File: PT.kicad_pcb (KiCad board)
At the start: 4 copper layers, 67 x 68 mm, 111 parts, among them J1 Conn_02x05_Odd_Even, J10 Conn_02x01, J11 Screw_Terminal_01x02, J2 USB_C_Receptacle_USB2.0_16P, J3 Conn_02x01, J4 Conn_02x01, J5 Screw_Terminal_01x05, J6 RJ45_Hanrun_HR911105A_Horizon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, J7 Conn_02x01, J8 Conn_02x01, J9 Conn_02x01, SW1 SKRPANE010, U1 USBLC6-2SC6, U2 STM32H563RIVx, U3 AP2112K-3.3, U4 TJA1042T-3, U5 LAN8742A, U6 ADS131A04, Y1 25 MHz, Y2 25 MHz, Y3 16.384 MHz

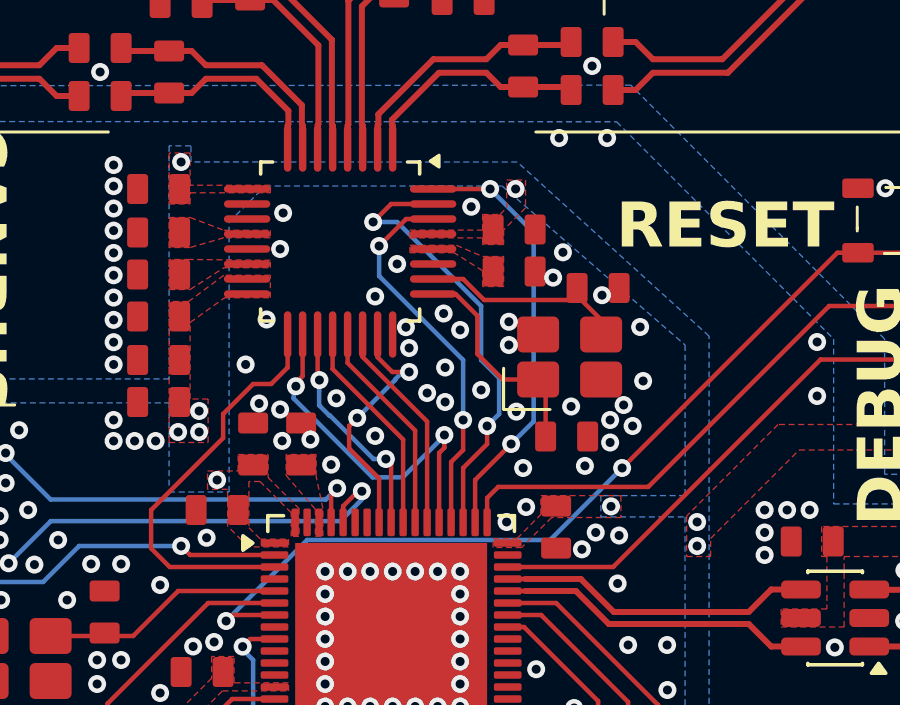
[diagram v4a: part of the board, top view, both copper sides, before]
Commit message: Use static configurations for ADC instead of using MCU for pullups/downs
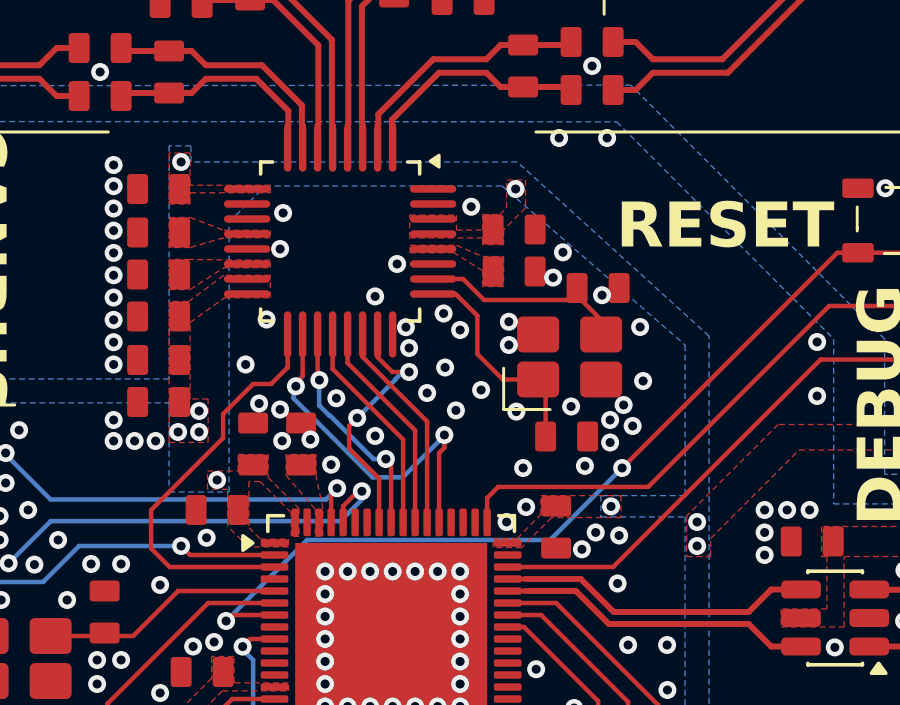
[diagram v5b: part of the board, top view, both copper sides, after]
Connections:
- net ETH_CRS_DV renamed /Connectivity/ETH_CRS_DV
- net ETH_MDC renamed /Connectivity/ETH_MDC
- net ETH_MDIO renamed /Connectivity/ETH_MDIO
- net ETH_REF_CLK renamed /Connectivity/ETH_REF_CLK
- net ETH_RXD0 renamed /Connectivity/ETH_RXD0
- net ETH_RXD1 renamed /Connectivity/ETH_RXD1
- net ETH_TXD0 renamed /Connectivity/ETH_TXD0
- net ETH_TXD1 renamed /Connectivity/ETH_TXD1
- net ETH_TX_EN renamed /Connectivity/ETH_TX_EN
- net ETH_~{RST} renamed /Connectivity/ETH_~{RST}
- net FDCAN_RX renamed /Connectivity/FDCAN_RX
- net FDCAN_STDBY renamed /Connectivity/FDCAN_STDBY
- net FDCAN_TX renamed /Connectivity/FDCAN_TX
- net MISO renamed /Analog/MISO
- net MOSI renamed /Analog/MOSI
- net SCLK renamed /Analog/SCLK
- net ~{ADC_RESET} renamed /Analog/~{ADC_RESET}
- net ~{CS} renamed /Analog/~{CS}
- net ~{DONE} renamed /Analog/~{DONE}
- net ~{DRDY} renamed /Analog/~{DRDY}
- U2 pad 53: M2 -> unconnected-(U2-PA15(JTDI)-Pad53)
- U2 pad 54: M1 -> unconnected-(U2-PC10-Pad54)
- U2 pad 55: M0 -> unconnected-(U2-PC11-Pad55)
- U6 pad 30: M0 -> +3.3V
- U6 pad 31: M1 -> GND
- U6 pad 32: M2 -> GND
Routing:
- net M1: track 15.0 -> 0.00 mm, vias 2 -> 0
- net M2: track 14.4 -> 0.00 mm, vias 2 -> 0
- net M0: track 12.7 -> 0.00 mm, vias 2 -> 0

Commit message: holy hell 2 adcs
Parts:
- added C43: 10nF, APRLPrints:C_0603, F.Cu at (106.9, 103.5)
- added C44: 100nF, APRLPrints:C_0603, F.Cu at (111.5, 120.0)
- added C45: 100nF, APRLPrints:C_0603, F.Cu at (113.3, 107.4)
- added C46: 100nF, APRLPrints:C_0603, F.Cu at (116.3, 120.0)
- added C47: 100nF, APRLPrints:C_0603, F.Cu at (117.9, 120.0)
- added C48: 1uF, APRLPrints:C_0603, F.Cu at (119.5, 120.0)
- added C49: 1uF, APRLPrints:C_0603, F.Cu at (113.1, 120.0)
- added C50: 10nF, APRLPrints:C_0603, F.Cu at (106.7, 110.2)
- added C51: 1uF, APRLPrints:C_0603, F.Cu at (114.7, 120.0)
- added C52: 1uF, APRLPrints:C_0603, F.Cu at (114.9, 107.4)
- added C53: 10nF, APRLPrints:C_0603, F.Cu at (106.7, 117.1)
- added C54: 30pF, APRLPrints:C_0603, F.Cu at (117.9, 105.3)
- added C55: 30pF, APRLPrints:C_0603, F.Cu at (120.3, 108.1)
- added C56: 10nF, APRLPrints:C_0603, F.Cu at (106.7, 124.0)
- added F4: 100mA Hold, APRLPrints:Fuse_0805_2012Metric, F.Cu at (120.5, 73.3)
- added F5: 500mA, APRLPrints:Fuse_0805_2012Metric, F.Cu at (170.9, 85.0)
- added J12: Conn_01x04, Connector_PinHeader_2.54mm:PinHeader_1x04_P2.54mm_Vertical, F.Cu at (147.1, 99.1)
- added J13: Conn_02x01, TerminalBlock_Phoenix:TerminalBlock_Phoenix_MPT-0,5-2-2.54_1x02_P2.54mm_Horizontal, F.Cu at (96.8, 102.2)
- added J14: Conn_02x01, TerminalBlock_Phoenix:TerminalBlock_Phoenix_MPT-0,5-2-2.54_1x02_P2.54mm_Horizontal, F.Cu at (96.8, 108.9)
- added J15: Conn_02x01, TerminalBlock_Phoenix:TerminalBlock_Phoenix_MPT-0,5-2-2.54_1x02_P2.54mm_Horizontal, F.Cu at (96.8, 115.8)
- added J16: Conn_02x01, TerminalBlock_Phoenix:TerminalBlock_Phoenix_MPT-0,5-2-2.54_1x02_P2.54mm_Horizontal, F.Cu at (96.8, 122.8)
- added J17: Screw_Terminal_01x02, TerminalBlock_Phoenix:TerminalBlock_Phoenix_MPT-0,5-2-2.54_1x02_P2.54mm_Horizontal, F.Cu at (128.5, 77.4)
- added J18: Conn_01x05, Connector_PinHeader_2.54mm:PinHeader_1x05_P2.54mm_Vertical, F.Cu at (157.4, 103.3)
- added NT5: NetTie_2, NetTie:NetTie-2_SMD_Pad0.5mm, F.Cu at (102.1, 102.1)
- added NT6: NetTie_2, NetTie:NetTie-2_SMD_Pad0.5mm, F.Cu at (102.1, 108.7)
- added NT7: NetTie_2, NetTie:NetTie-2_SMD_Pad0.5mm, F.Cu at (102.1, 115.7)
- added NT8: NetTie_2, NetTie:NetTie-2_SMD_Pad0.5mm, F.Cu at (102.1, 122.5)
- added R32: 100R, APRLPrints:R_0603, F.Cu at (104.7, 104.2)
- added R33: 100R, APRLPrints:R_0805, F.Cu at (102.1, 103.5)
- added R34: 100R, APRLPrints:R_0603, F.Cu at (104.7, 102.7)
- added R35: 100R, APRLPrints:R_0603, F.Cu at (104.5, 111.0)
- added R36: 100R, APRLPrints:R_0805, F.Cu at (102.1, 110.2)
- added R37: 100R, APRLPrints:R_0603, F.Cu at (104.5, 109.4)
- added R38: 100R, APRLPrints:R_0603, F.Cu at (104.5, 117.9)
- added R39: 100R, APRLPrints:R_0805, F.Cu at (102.1, 117.0)
- added R40: 100R, APRLPrints:R_0603, F.Cu at (104.5, 116.3)
- added R41: 100R, APRLPrints:R_0603, F.Cu at (104.5, 124.8)
- added R42: 100R, APRLPrints:R_0805, F.Cu at (102.1, 124.0)
- added R43: 100R, APRLPrints:R_0603, F.Cu at (104.5, 123.2)
- added R44: 10k, APRLPrints:R_0603, F.Cu at (144.5, 98.5)
- added R45: 10k, APRLPrints:R_0603, F.Cu at (142.9, 97.5)
- added U7: ADS131A04, libpt:QFP-32_5x5_Pitch0.5mm, F.Cu at (115.3, 113.7)
- added Y4: 16.384 MHz, APRLPrints:3225-4P-L, F.Cu at (120.5, 105.1)
- F2: value 100mA Hold -> 500mA
- J11: value Screw_Terminal_01x02 -> Conn_02x01
- J3: value Conn_02x01 -> Screw_Terminal_01x02; footprint Connector_PinHeader_2.54mm:PinHeader_2x01_P2.54mm_Vertical -> TerminalBlock_Phoenix:TerminalBlock_Phoenix_MPT-0,5-2-2.54_1x02_P2.54mm_Horizontal
- J5: value Screw_Terminal_01x05 -> Conn_02x01; footprint TerminalBlock_Phoenix:TerminalBlock_Phoenix_MPT-0,5-5-2.54_1x05_P2.54mm_Horizontal -> Connector_PinHeader_2.54mm:PinHeader_2x01_P2.54mm_Vertical
- J6: value RJ45_Hanrun_HR911105A_Horizontal -> Screw_Terminal_01x05; footprint Connector_RJ:RJ45_Hanrun_HR911105A_Horizontal -> TerminalBlock_Phoenix:TerminalBlock_Phoenix_MPT-0,5-5-2.54_1x05_P2.54mm_Horizontal
- J7: value Conn_02x01 -> RJ45_Hanrun_HR911105A_Horizontal; footprint TerminalBlock_Phoenix:TerminalBlock_Phoenix_MPT-0,5-2-2.54_1x02_P2.54mm_Horizontal -> Connector_RJ:RJ45_Hanrun_HR911105A_Horizontal
- R9: moved to F.Cu
- moved R19 78.2 mm to (179.5, 128.4), turned to 0 degrees
- moved R18 77.5 mm to (180.0, 109.3)
- moved R17 73.9 mm to (176.7, 128.4), turned to 180 degrees
- moved J6 71.8 mm to (176.7, 84.1), turned to 90 degrees
- moved H2 70.6 mm to (135.3, 75.3)
- moved J3 68.8 mm to (176.8, 91.3), turned to 90 degrees
- moved J5 68.2 mm to (167.4, 79.5), turned to 0 degrees
- moved J4 68.1 mm to (170.0, 75.8), turned to 180 degrees
- moved R9 64.7 mm to (164.5, 77.7), turned to -90 degrees
- moved J11 61.8 mm to (96.8, 95.3), turned to -90 degrees
- moved C25 50.9 mm to (159.2, 81.3), turned to 180 degrees
- moved NT1 49.8 mm to (102.1, 74.3), turned to -90 degrees
- moved U4 49.6 mm to (159.1, 77.7), turned to 0 degrees
- moved R21 48.2 mm to (102.1, 76.0), turned to 90 degrees
- moved J7 47.6 mm to (166.2, 123.3), turned to 90 degrees
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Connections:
- net /Analog/AIN1+ renamed /ADC 1/AIN1+
- net /Analog/AIN1- renamed /ADC 1/AIN1-
- net /Analog/AIN1_SENSE- renamed /ADC 1/AIN1_SENSE-
- net /Analog/AIN2+ renamed /ADC 1/AIN2+
- net /Analog/AIN2- renamed /ADC 1/AIN2-
- net /Analog/AIN2_SENSE- renamed /ADC 1/AIN2_SENSE-
- net /Analog/AIN3+ renamed /ADC 1/AIN3+
- net /Analog/AIN3- renamed /ADC 1/AIN3-
- net /Analog/AIN3_SENSE- renamed /ADC 1/AIN3_SENSE-
- net /Analog/AIN4+ renamed /ADC 1/AIN4+
- net /Analog/AIN4- renamed /ADC 1/AIN4-
- net /Analog/AIN4_SENSE- renamed /ADC 1/AIN4_SENSE-
- net /Analog/MISO renamed /ADC 1/MISO
- net /Analog/MOSI renamed /ADC 1/MOSI
- net /Analog/SCLK renamed /ADC 1/SCLK
- net /Analog/~{DRDY} renamed /ADC 1/~{DRDY}
- F2 pad 1: +24V -> Net-(J3-Pin_2)
- F2 pad 2: Net-(J11-Pin_2) -> +5V
- J10 pad 2: /Analog/AIN4_SENSE+ -> /ADC 1/AIN3_SENSE+
- J11 pad 1: GND -> +24V
- J11 pad 2: Net-(J11-Pin_2) -> /ADC 1/AIN4_SENSE+
- J3 pad 1: /Connectivity/CAN+ -> GND
- J4 pad 1: Net-(J4-Pin_1) -> /Connectivity/CAN+
- J4 pad 2: /Connectivity/CAN- -> Net-(J4-Pin_2)
- J5 pad 1: +3.3V -> Net-(J5-Pin_1)
- J5 pad 2: +5V -> /Connectivity/CAN-
- J6 pad 1: /Connectivity/TX+ -> Net-(J6-Pin_1)
- J6 pad 2: /Connectivity/TX- -> +3.3V
- J6 pad 3: /Connectivity/RX+ -> /Connectivity/CAN-
- J6 pad 4: +3.3V -> /Connectivity/CAN+
- J6 pad 5: +3.3V -> GND
- J7 pad 1: +24V -> /Connectivity/TX+
- J7 pad 2: /Analog/AIN1_SENSE+ -> /Connectivity/TX-
- J8 pad 2: /Analog/AIN2_SENSE+ -> /ADC 1/AIN1_SENSE+
- J9 pad 2: /Analog/AIN3_SENSE+ -> /ADC 1/AIN2_SENSE+
- R18 pad 1: Net-(J6-Pad11) -> Net-(J7-Pad11)
- R19 pad 1: Net-(J6-Pad10) -> Net-(J7-Pad10)
- R20 pad 1: /Analog/AIN1_SENSE+ -> /ADC 1/AIN1_SENSE+
- R21 pad 1: /Analog/AIN1_SENSE+ -> /ADC 1/AIN1_SENSE+
- R23 pad 1: /Analog/AIN2_SENSE+ -> /ADC 1/AIN2_SENSE+
- R24 pad 1: /Analog/AIN2_SENSE+ -> /ADC 1/AIN2_SENSE+
- R26 pad 1: /Analog/AIN3_SENSE+ -> /ADC 1/AIN3_SENSE+
- R27 pad 1: /Analog/AIN3_SENSE+ -> /ADC 1/AIN3_SENSE+
- R29 pad 1: /Analog/AIN4_SENSE+ -> /ADC 1/AIN4_SENSE+
- R30 pad 1: /Analog/AIN4_SENSE+ -> /ADC 1/AIN4_SENSE+
- R9 pad 1: Net-(J3-Pin_2) -> Net-(J4-Pin_2)
- R9 pad 2: Net-(J4-Pin_1) -> Net-(J5-Pin_1)
- U2 pad 2: /Connectivity/FDCAN_STDBY -> /ADC 1/~{ADC_RESET}
- U2 pad 20: unconnected-(U2-PA4-Pad20) -> /ADC 2/~{DRDY}
- U2 pad 21: unconnected-(U2-PA5-Pad21) -> /ADC 2/~{DONE}
- U2 pad 22: unconnected-(U2-PA6-Pad22) -> /ADC 2/~{ADC_RESET}
- U2 pad 26: unconnected-(U2-PB0-Pad26) -> /Microcontroller/USER_LED_1
- U2 pad 27: unconnected-(U2-PB1-Pad27) -> /Microcontroller/USER_LED_2
- U2 pad 28: unconnected-(U2-PB2-Pad28) -> /Microcontroller/USER_LED_3
- U2 pad 3: /Analog/~{ADC_RESET} -> unconnected-(U2-PC14-Pad3)
- U2 pad 38: unconnected-(U2-PD11-Pad38) -> /Microcontroller/GPIO5
- U2 pad 39: unconnected-(U2-PD12-Pad39) -> /Microcontroller/GPIO4
- U2 pad 40: unconnected-(U2-PC6-Pad40) -> /Microcontroller/GPIO3
- U2 pad 41: unconnected-(U2-PC7-Pad41) -> /Microcontroller/GPIO2
- U2 pad 42: unconnected-(U2-PC8-Pad42) -> /Microcontroller/GPIO1
- U2 pad 43: unconnected-(U2-PC9-Pad43) -> /Microcontroller/I2C_SDA
- U2 pad 44: /Microcontroller/USER_LED_1 -> /Microcontroller/I2C_SCL
- U2 pad 45: /Microcontroller/USER_LED_2 -> unconnected-(U2-PA9-Pad45)
- U2 pad 46: /Microcontroller/USER_LED_3 -> unconnected-(U2-PA10-Pad46)
- U2 pad 56: /Analog/~{DONE} -> /ADC 1/~{CS}
- U2 pad 61: /Analog/~{CS} -> /ADC 1/~{DONE}
- U2 pad 8: unconnected-(U2-PC0-Pad8) -> /ADC 2/~{CS}
- U6 pad 17: /Analog/~{ADC_RESET} -> /ADC 1/~{ADC_RESET}
- U6 pad 18: /Analog/~{DONE} -> /ADC 1/~{DONE}
- U6 pad 23: /Analog/~{CS} -> /ADC 1/~{CS}
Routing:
- net /ADC 1/MOSI: track 7.24 -> 59.6 mm, vias 0 -> 2
- net /ADC 1/MISO: track 7.19 -> 58.1 mm, vias 0 -> 2
- net /ADC 1/SCLK: track 7.15 -> 56.5 mm, vias 0 -> 2
- net /Connectivity/ETH_MDC: track 16.1 -> 49.4 mm
- net /Connectivity/ETH_~{RST}: track 15.1 -> 45.3 mm
- net /Connectivity/ETH_REF_CLK: track 14.1 -> 41.2 mm
- net /ADC 1/~{CS}: track 0.00 -> 25.9 mm
- net /ADC 2/~{ADC_RESET}: track 0.00 -> 25.2 mm, vias 0 -> 2
- net /ADC 2/~{CS}: track 0.00 -> 24.5 mm
- net +5V: track 0.00 -> 24.5 mm, vias 10 -> 4
- net /ADC 2/~{DONE}: track 0.00 -> 22.8 mm, vias 0 -> 2
- net /ADC 1/~{DONE}: track 0.00 -> 21.7 mm
- net /Connectivity/ETH_MDIO: track 15.3 -> 36.7 mm, vias 2 -> 0
- net /ADC 2/~{DRDY}: track 0.00 -> 21.2 mm, vias 0 -> 2
- net /Connectivity/ETH_TX_EN: track 16.4 -> 37.2 mm
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- added copper zone on F.Cu, net (none)
- added copper zone on F.Cu, net /ADC 1/AIN1_SENSE+
- added copper zone on F.Cu, net /ADC 1/AIN2_SENSE+
- added copper zone on F.Cu, net /ADC 1/AIN3_SENSE+
- added copper zone on F.Cu, net /ADC 1/AIN4_SENSE+
- added copper zone on F.Cu, net /ADC 2/AIN1_SENSE+
- added copper zone on F.Cu, net /ADC 2/AIN2_SENSE+
- added copper zone on F.Cu, net /ADC 2/AIN3_SENSE+
- added copper zone on F.Cu, net /ADC 2/AIN4_SENSE+
- added copper zone on F.Cu, net /Microcontroller/+24_IN
- added copper zone on F.Cu, net Net-(J3-Pin_2)
- added copper zone on F.Cu, net Net-(U7-CAP)
- added copper zone on F.Cu, net Net-(U7-REFEXT)
- added copper zone on F.Cu, net Net-(U7-REFP)
- removed copper zone on B.Cu, net +5V
- removed copper zone on F.Cu, net /Analog/AIN1_SENSE+
- removed copper zone on F.Cu, net /Analog/AIN2_SENSE+
- removed copper zone on F.Cu, net /Analog/AIN3_SENSE+
- removed copper zone on F.Cu, net /Analog/AIN4_SENSE+
- removed copper zone on F.Cu, net Net-(J11-Pin_2)
- removed copper zone on F.Cu, net Net-(J2-CC1)
- removed copper zone on F.Cu, net Net-(J2-CC2)
- removed copper zone on F.Cu, net Net-(U5-VDDCR)
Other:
- board size 67 x 68 mm -> 91 x 60 mm
- board text added: "1-1"
- board text added: "1-2"
- board text added: "1-3"
- board text added: "1-4"
- board text added: "2-1"
- board text added: "2-2"
- board text added: "2-3"
- board text added: "2-4"
- board text added: "3V3"
- board text added: "5V"
- board text added: "C+"
- board text added: "C-"
- board text added: "Designed By: Nolan Poe Reviewed By: Daniel Fan"
- board text added: "FAST ETH"
- board text added: "GND"
- board text added: "I2C + GPIO"
- board text added: "PB0"
- board text added: "PB1"
- board text added: "PB2"
- board text added: "REV 1A"
- board text added: "USB"
- board text added: "{dblquote}MEANIE{dblquote}"
- board text removed: "+3.3V/+5V STATUS"
- board text removed: "1"
- board text removed: "2"
- board text removed: "3"
- board text removed: "4"
- board text removed: "BY: NOLAN POE"
- board text removed: "CANBUS"
- board text removed: "FAST ETHERNET"
- board text removed: "GND CAN+ CAN- +5V +3.3V"
- board text removed: "PA10"
- board text removed: "PA8"
- board text removed: "PA9"
- board text removed: "UNDER NORMAL OPERATION, ONLY USE INTERAL +3.3V EXTERNAL +3.3V IS UNFUSED AND UNFILTERED AND BACKFLOWS TO +5V"
